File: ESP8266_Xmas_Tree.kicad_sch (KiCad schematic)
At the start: 16 parts, among them U1 WeMos_D1_mini

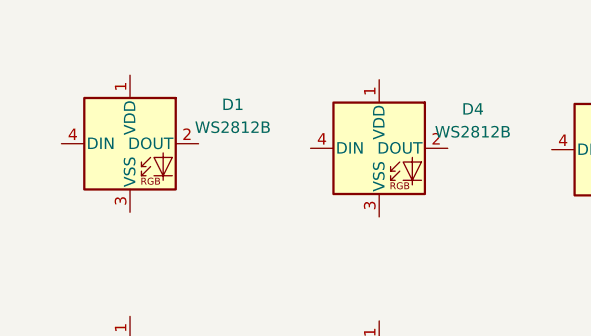
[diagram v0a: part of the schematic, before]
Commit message: adding d1 mini step model to pcb
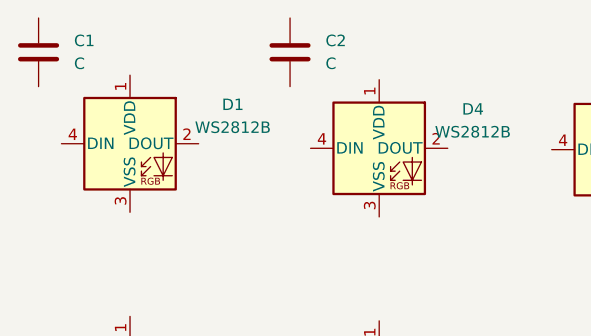
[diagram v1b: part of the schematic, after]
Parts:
- added C1, C2: C, Capacitor_SMD:C_0805_2012Metric_Pad1.18x1.45mm_HandSolder, symbol Device:C
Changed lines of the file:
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@@
     (pin "4")
+  )
+  (symbol (lib_id "Device:C") (at 24.003 22.479 0) (unit 1)
+    (in_bom yes) (on_board yes) (fields_autoplaced)
+    (property "Reference" "C1" (id 0) (at 27.94 21.2089 0)
+      (effects (font (size 1.27 1.27)) (justify left))
+    )
+    (property "Value" "C" (id 1) (at 27.94 23.7489 0)
+      (effects (font (size 1.27 1.27)) (justify left))
+    )
+    (property "Footprint" "Capacitor_SMD:C_0805_2012Metric_Pad1.18x1.45mm_HandSolder" (id 2) (at 24.9682 26.289 0)
+      (effects (font (size 1.27 1.27)) hide)
+    )
+    (property "Datasheet" "~" (id 3) (at 24.003 22.479 0)
+      (effects (font (size 1.27 1.27)) hide)
+    )
+    (pin "1")
+    (pin "2")
   )
   (symbol (lib_id "MCU_Module:WeMos_D1_mini") (at 57.15 144.272 0) (unit 1)
@@
     (pin "4")
   )
+  (symbol (lib_id "Device:C") (at 51.943 22.479 0) (unit 1)
+    (in_bom yes) (on_board yes) (fields_autoplaced)
+    (property "Reference" "C2" (id 0) (at 55.88 21.2089 0)
+      (effects (font (size 1.27 1.27)) (justify left))
+    )
+    (property "Value" "C" (id 1) (at 55.88 23.7489 0)
+      (effects (font (size 1.27 1.27)) (justify left))
+    )
+    (property "Footprint" "Capacitor_SMD:C_0805_2012Metric_Pad1.18x1.45mm_HandSolder" (id 2) (at 52.9082 26.289 0)
+      (effects (font (size 1.27 1.27)) hide)
+    )
+    (property "Datasheet" "~" (id 3) (at 51.943 22.479 0)
+      (effects (font (size 1.27 1.27)) hide)
+    )
+    (pin "1")
+    (pin "2")
+  )
   (symbol (lib_id "LED:WS2812B") (at 34.163 32.639 0) (unit 1)
     (in_bom yes) (on_board yes) (fields_autoplaced)
@@
   )
   (symbol_instances
+    (path "/36d9a2cd-afc9-4172-8e56-b2cfc968cbec"
+      (reference "C1") (unit 1) (value "C") (footprint "Capacitor_SMD:C_0805_2012Metric_Pad1.18x1.45mm_HandSolder")
+    )
+    (path "/c4ce4eab-9390-4c62-81ee-16886c116800"
+      (reference "C2") (unit 1) (value "C") (footprint "Capacitor_SMD:C_0805_2012Metric_Pad1.18x1.45mm_HandSolder")
+    )
     (path "/e58840a6-e6ee-44de-860d-d7e09469d7c3"
       (reference "D1") (unit 1) (value "WS2812B") (footprint "LED_SMD:LED_WS2812B_PLCC4_5.0x5.0mm_P3.2mm")

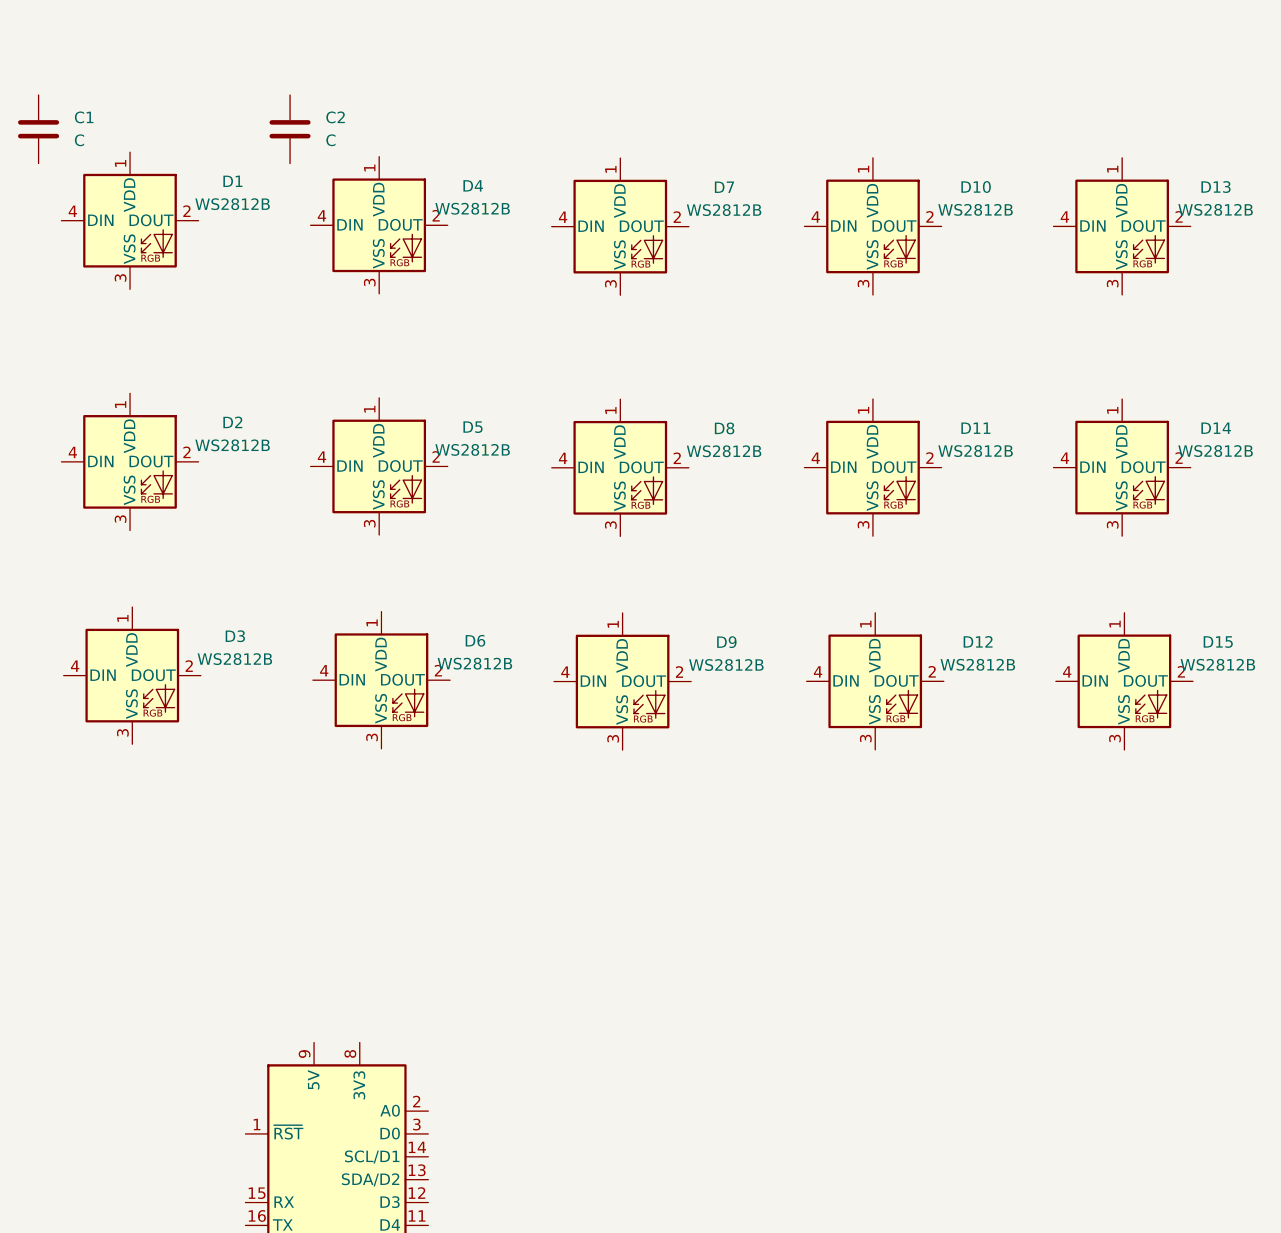
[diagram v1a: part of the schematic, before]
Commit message: adding caps for WS2812B LEDs
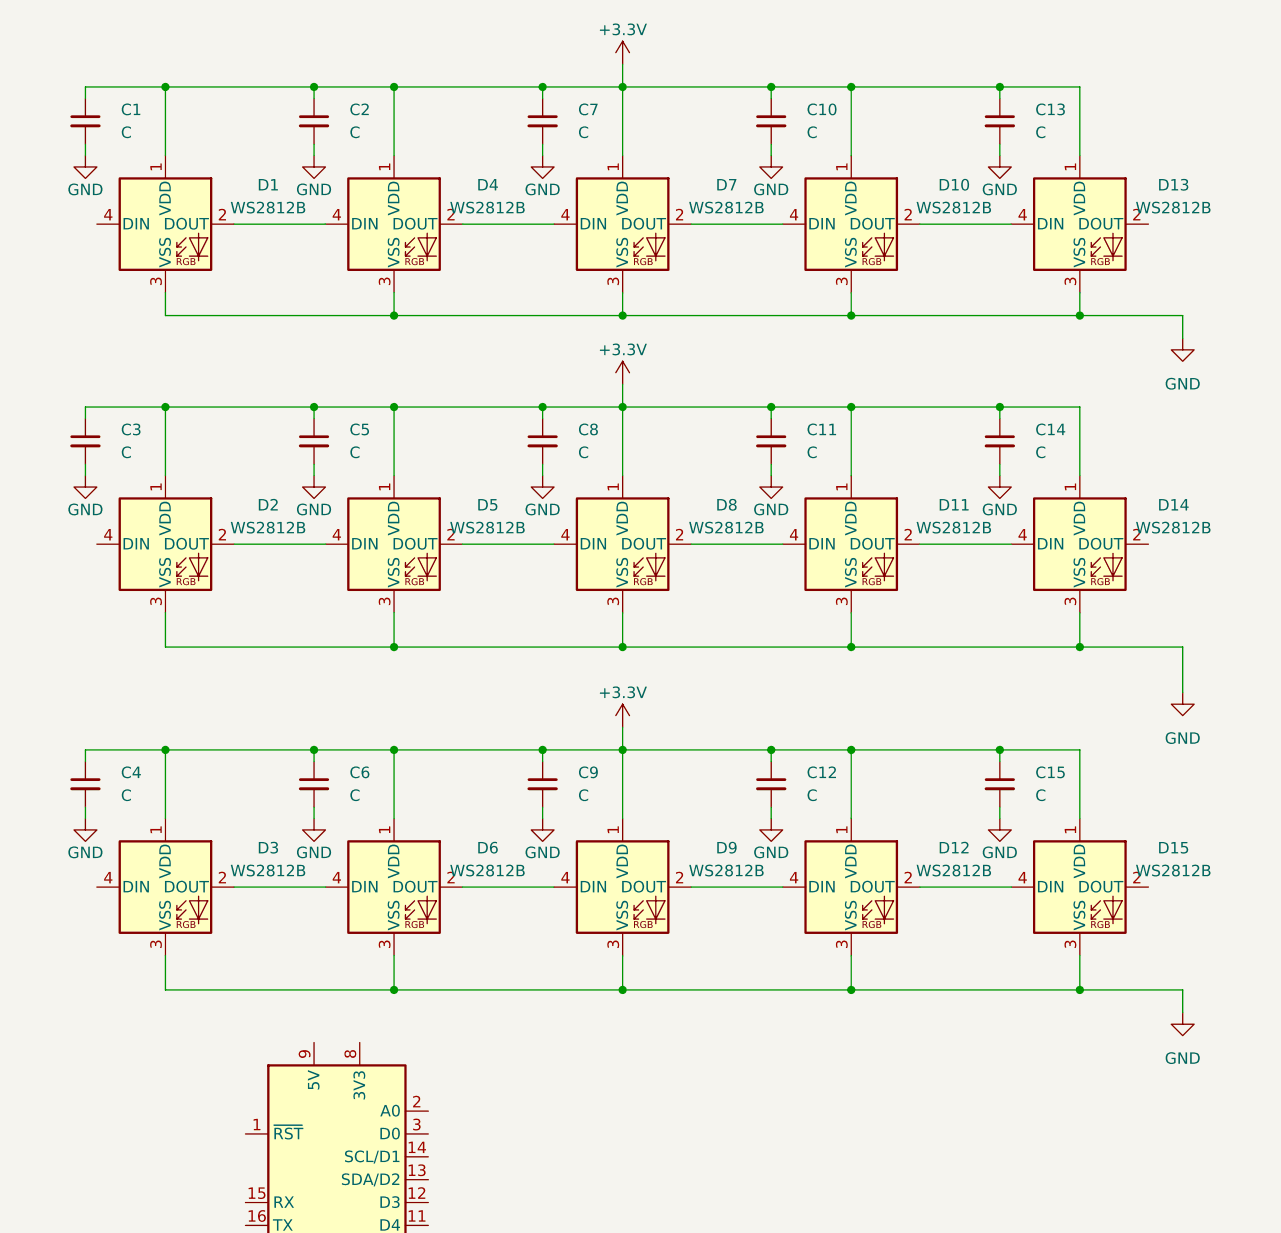
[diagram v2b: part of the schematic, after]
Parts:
- added C10, C11, C12, C13, C14, C15, C3, C4, C5, C6, C7, C8, C9: C, Capacitor_SMD:C_0805_2012Metric_Pad1.18x1.45mm_HandSolder, symbol Device:C_Small
- C1, C2: symbol Device:C -> Device:C_Small
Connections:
- net +3.3V: now reaches D8.1 (VDD)
- net +3.3V: now also C1.1, C2.1, D1.1 (VDD), D10.1 (VDD), D11.1 (VDD), D12.1 (VDD), D13.1 (VDD), D14.1 (VDD), D15.1 (VDD), D2.1 (VDD), D3.1 (VDD), D4.1 (VDD), D5.1 (VDD), D6.1 (VDD), D7.1 (VDD), D9.1 (VDD), C10.1, C11.1, C12.1, C13.1, C14.1, C15.1, C3.1, C4.1, C5.1, C6.1, C7.1, C8.1, C9.1
- net at D8.2 (DOUT): now also D11.4 (DIN)
- net GND: now reaches D8.3 (VSS)
- net GND: now also C1.2, C2.2, D1.3 (VSS), D10.3 (VSS), D11.3 (VSS), D12.3 (VSS), D13.3 (VSS), D14.3 (VSS), D15.3 (VSS), D2.3 (VSS), D3.3 (VSS), D4.3 (VSS), D5.3 (VSS), D6.3 (VSS), D7.3 (VSS), D9.3 (VSS), C10.2, C11.2, C12.2, C13.2, C14.2, C15.2, C3.2, C4.2, C5.2, C6.2, C7.2, C8.2, C9.2
- net at D8.4 (DIN): now also D5.2 (DOUT)
- net at D3.2 (DOUT): now also D6.4 (DIN)
- net at D11.2 (DOUT): now also D14.4 (DIN)
- net at D15.4 (DIN): now also D12.2 (DOUT)
- net at D6.2 (DOUT): now also D9.4 (DIN)
- net at D5.4 (DIN): now also D2.2 (DOUT)
- net at D13.4 (DIN): now also D10.2 (DOUT)
- net at D10.4 (DIN): now also D7.2 (DOUT)
- net at D9.2 (DOUT): now also D12.4 (DIN)
- net at D7.4 (DIN): now also D4.2 (DOUT)
- net at D4.4 (DIN): now also D1.2 (DOUT)
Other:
- moved on the sheet: C1, C2, D1, D10, D11, D12, D13, D14, D15, D2, D3, D4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

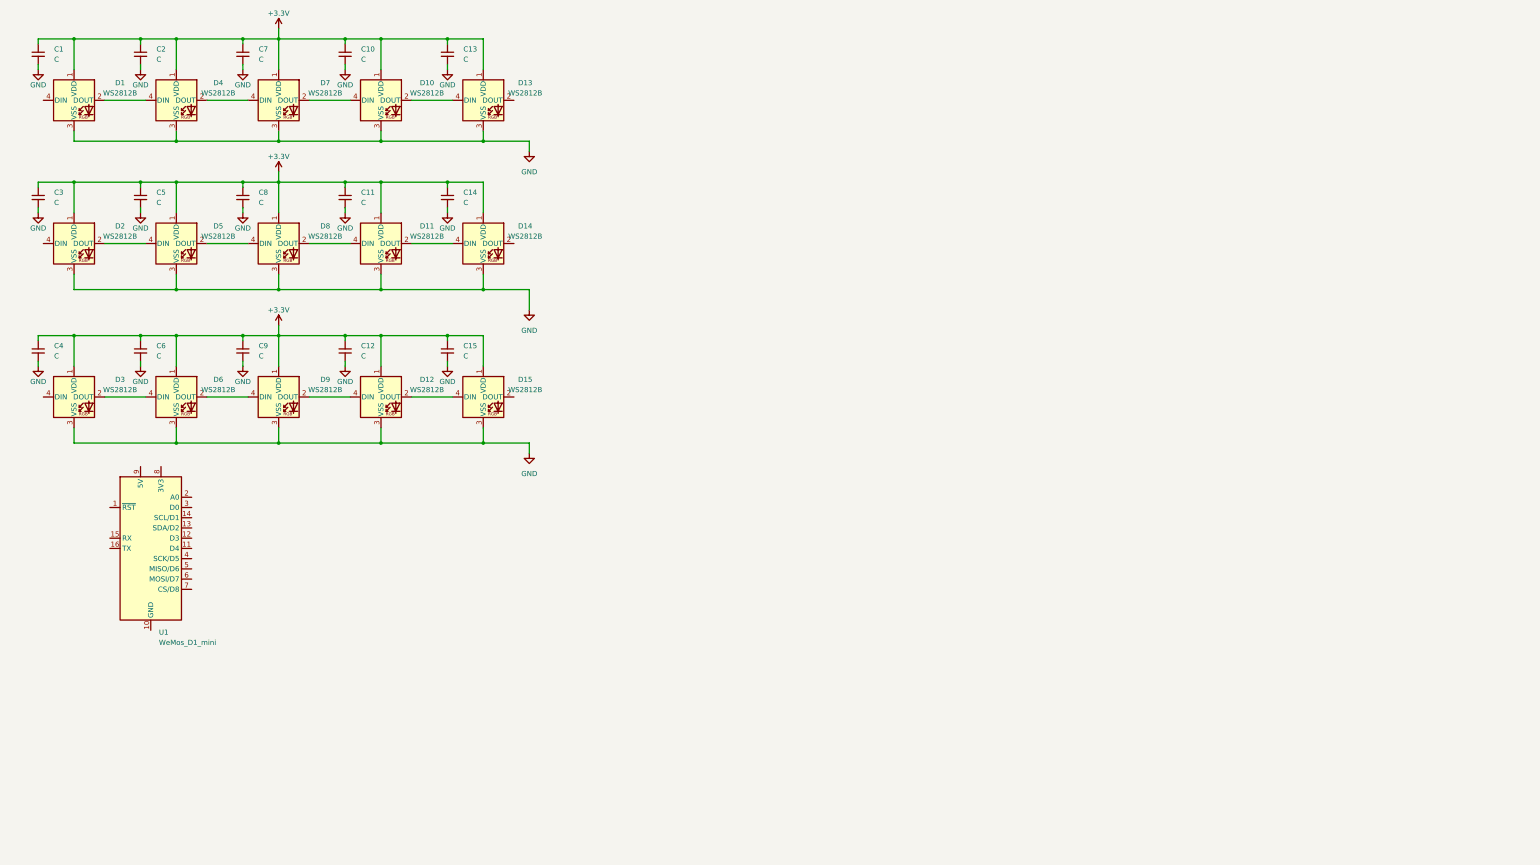
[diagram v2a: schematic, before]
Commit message: adding 3V3 and GND to MCU
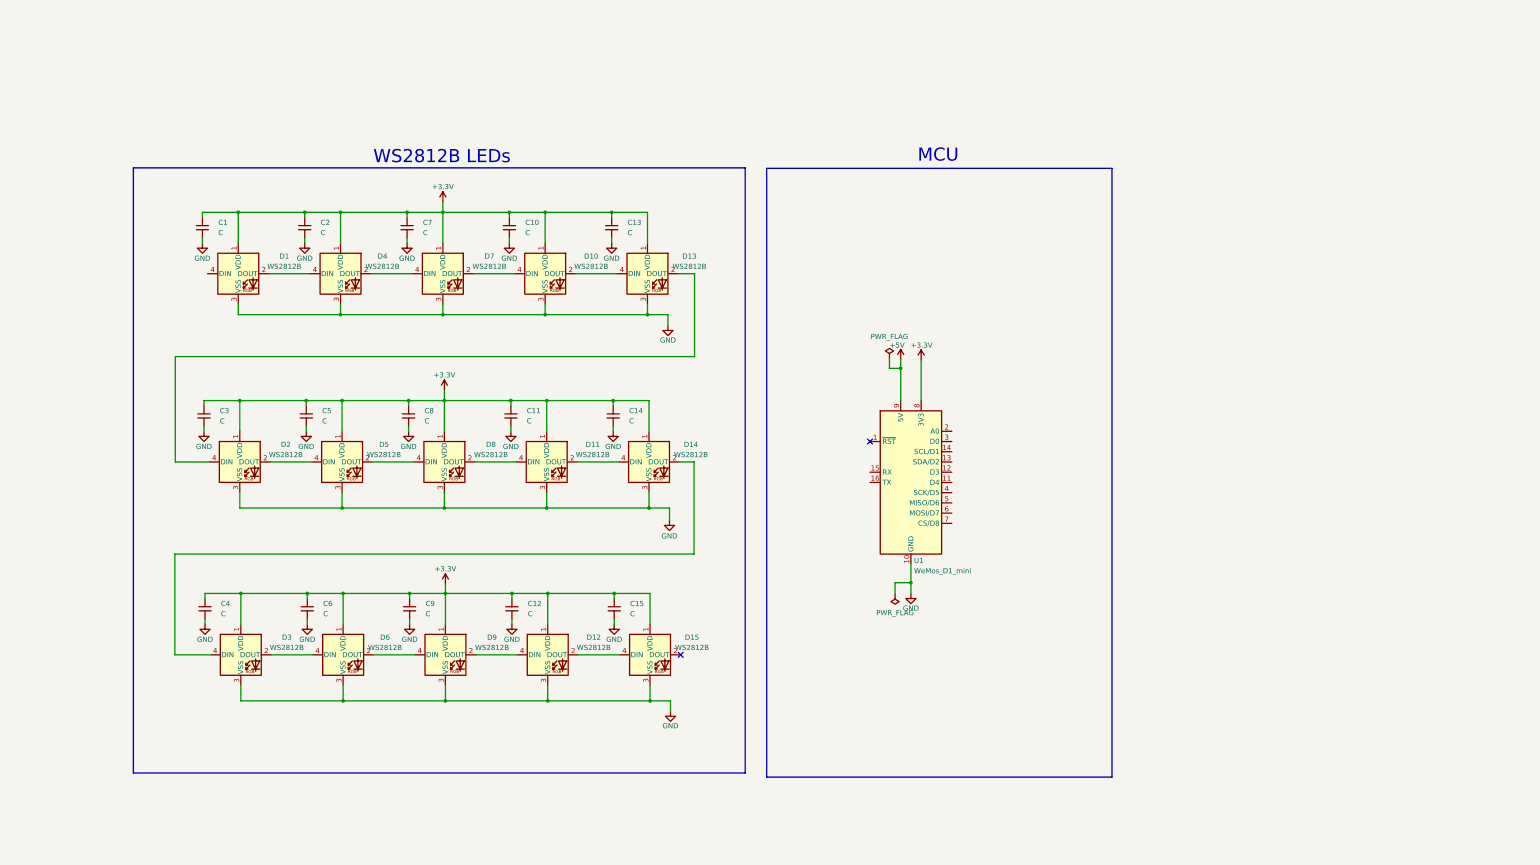
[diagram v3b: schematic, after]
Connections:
- net +3.3V: now also U1.8 (3V3)
- net GND: now also U1.10 (GND)
- net at D3.4 (DIN): now also D14.2 (DOUT)
- net +5V: now reaches U1.9 (5V)
- net at D13.2 (DOUT): now also D2.4 (DIN)
- no-connect marks 0 -> 2
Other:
- note added: "MCU"
- note added: "WS2812B LEDs"
- moved on the sheet: C1, C10, C11, C12, C13, C14, C15, C2, C3, C4, C5, C6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

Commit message: Fix the naming error of the capacitors and change the supply voltage from 3V3 to 5V of the LEDs.
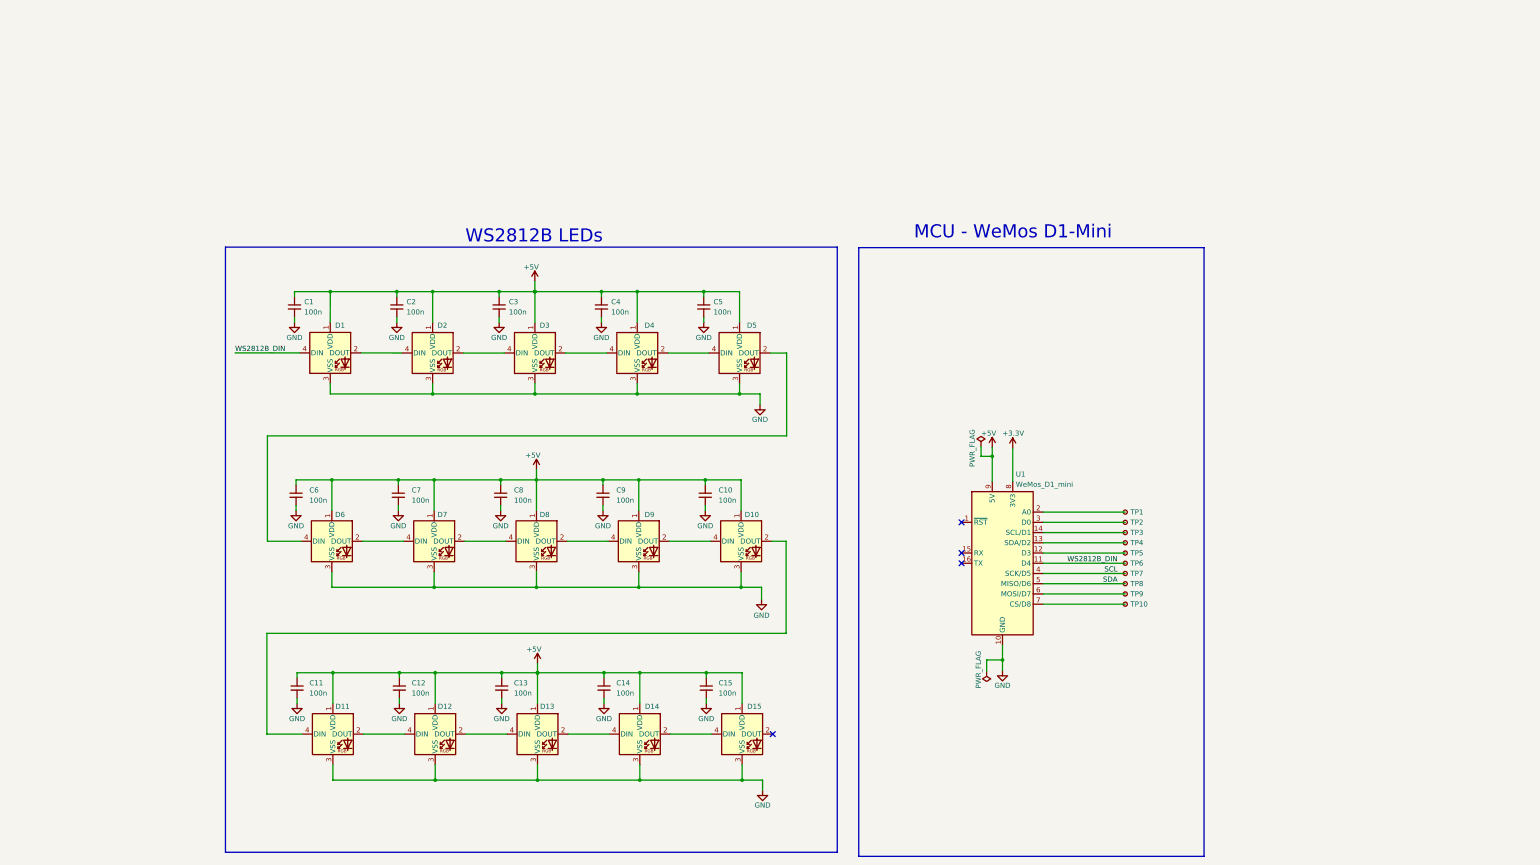
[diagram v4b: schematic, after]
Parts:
- added TP1, TP10, TP2, TP3, TP4, TP5, TP6, TP7, TP8, TP9: TestPoint_Small, TestPoint:TestPoint_Pad_D2.0mm, symbol Connector:TestPoint_Small
- C1, C15, C2, C8: value C -> 100n
- C10: renamed from C14; value C -> 100n
- C11: renamed from C4; value C -> 100n
- C12: renamed from C6; value C -> 100n
- C13: renamed from C9; value C -> 100n
- C14: renamed from C12; value C -> 100n
- C3: renamed from C7; value C -> 100n
- C4: renamed from C10; value C -> 100n
- C5: renamed from C13; value C -> 100n
- C6: renamed from C3; value C -> 100n
- C7: renamed from C5; value C -> 100n
- C9: renamed from C11; value C -> 100n
- renumbered D14 to D10, D3 to D11, D6 to D12, D9 to D13, D12 to D14, D4 to D2, D7 to D3, D10 to D4, D13 to D5, D2 to D6, D5 to D7, D11 to D9
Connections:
- net +3.3V: no longer C1.1, C10.1, C11.1, C12.1, C13.1, C14.1, C15.1, C2.1, C3.1, C4.1, C5.1, C6.1, C7.1, C8.1, C9.1, D1.1 (VDD), D10.1 (VDD), D11.1 (VDD), D12.1 (VDD), D13.1 (VDD), D14.1 (VDD), D15.1 (VDD), D2.1 (VDD), D3.1 (VDD), D4.1 (VDD), D5.1 (VDD), D6.1 (VDD), D7.1 (VDD), D8.1 (VDD), D9.1 (VDD)
- net +5V: now also C1.1, C10.1, C11.1, C12.1, C13.1, C14.1, C15.1, C2.1, C3.1, C4.1, C5.1, C6.1, C7.1, C8.1, C9.1, D1.1 (VDD), D10.1 (VDD), D11.1 (VDD), D12.1 (VDD), D13.1 (VDD), D14.1 (VDD), D15.1 (VDD), D2.1 (VDD), D3.1 (VDD), D4.1 (VDD), D5.1 (VDD), D6.1 (VDD), D7.1 (VDD), D8.1 (VDD), D9.1 (VDD)
- net WS2812B_DIN: now reaches U1.11 (D4)
- net WS2812B_DIN: now also D1.4 (DIN), TP6.1
- net at U1.12 (D3): now also TP5.1
- net at U1.13 (SDA/D2): now also TP4.1
- net at U1.14 (SCL/D1): now also TP3.1
- net at U1.2 (A0): now also TP1.1
- net at U1.3 (D0): now also TP2.1
- net SCL: now reaches U1.4 (SCK/D5)
- net SCL: now also TP7.1
- net SDA: now reaches U1.5 (MISO/D6)
- net SDA: now also TP8.1
- net at U1.6 (MOSI/D7): now also TP9.1
- net at U1.7 (CS/D8): now also TP10.1
- no-connect marks 2 -> 4
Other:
- note added: "MCU - WeMos D1-Mini"
- note removed: "MCU"
- moved on the sheet: C1, C10, C11, C12, C13, C14, C15, C2, C3, C4, C5, C6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
